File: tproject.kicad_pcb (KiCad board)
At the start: 2 copper layers, 28 parts, among them J1 USB_B_Micro, J2 Conn_01x04_Pin, J3 Conn_01x04_Pin, J4 Conn_01x04_Pin, SW1 SW_SPDT, U1 STM32F103C8T6, U2 AMS1117-3.3, Y1 16MHz

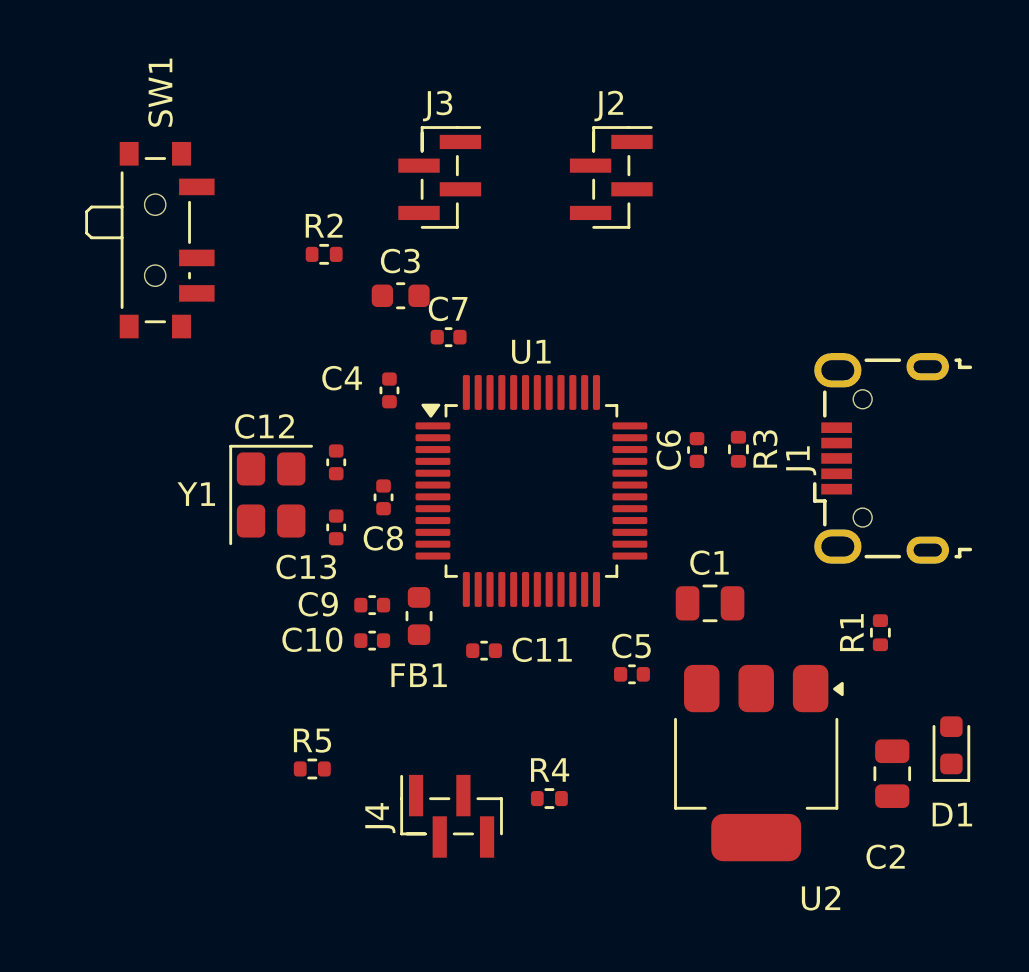
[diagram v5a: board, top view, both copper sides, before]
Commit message: Add board outline (38.54x33.17mm), 4x M2 mounting holes, adjust 8 components and add design note 0014
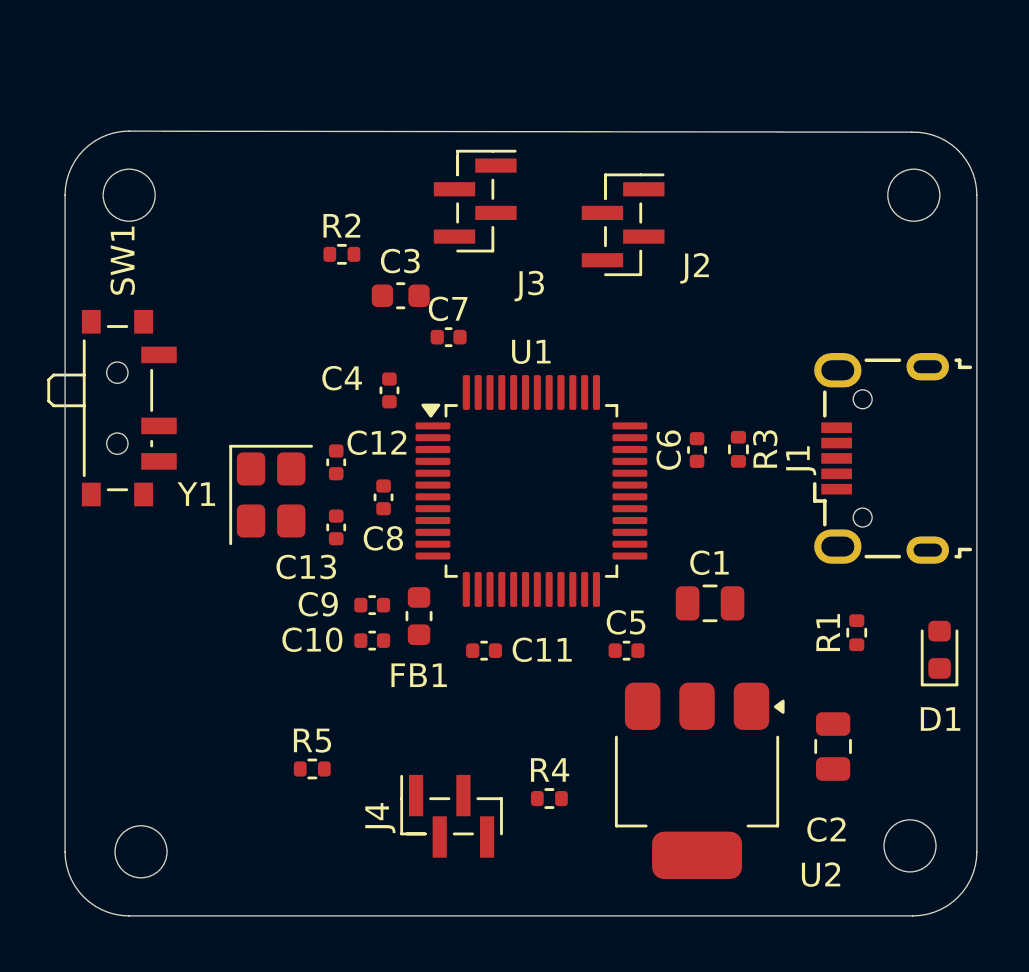
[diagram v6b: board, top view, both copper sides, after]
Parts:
- added H1: MountingHole, MountingHole:MountingHole_2.2mm_M2, F.Cu at (39.5, 82.5)
- added H2: MountingHole, MountingHole:MountingHole_2.2mm_M2, F.Cu at (39.0, 54.8)
- added H3: MountingHole, MountingHole:MountingHole_2.2mm_M2, F.Cu at (72.2, 54.8)
- added H4: MountingHole, MountingHole:MountingHole_2.2mm_M2, F.Cu at (72.0, 82.2)
- moved SW1 7.28 mm to (38.8, 63.8)
- moved D1 4.07 mm to (73.2, 74.0)
- moved C2 2.75 mm to (68.8, 78.0)
- moved U2 2.61 mm to (63.0, 79.5)
- moved J2 2.06 mm to (59.9, 56.0)
- moved J3 1.80 mm to (53.6, 55.0)
- moved C5 1.03 mm to (60.0, 74.0)
- moved R1 1.00 mm to (69.8, 73.2)
- moved R2 0.75 mm to (48.0, 57.2)
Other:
- board outline added: 38.5 x 33.2 mm

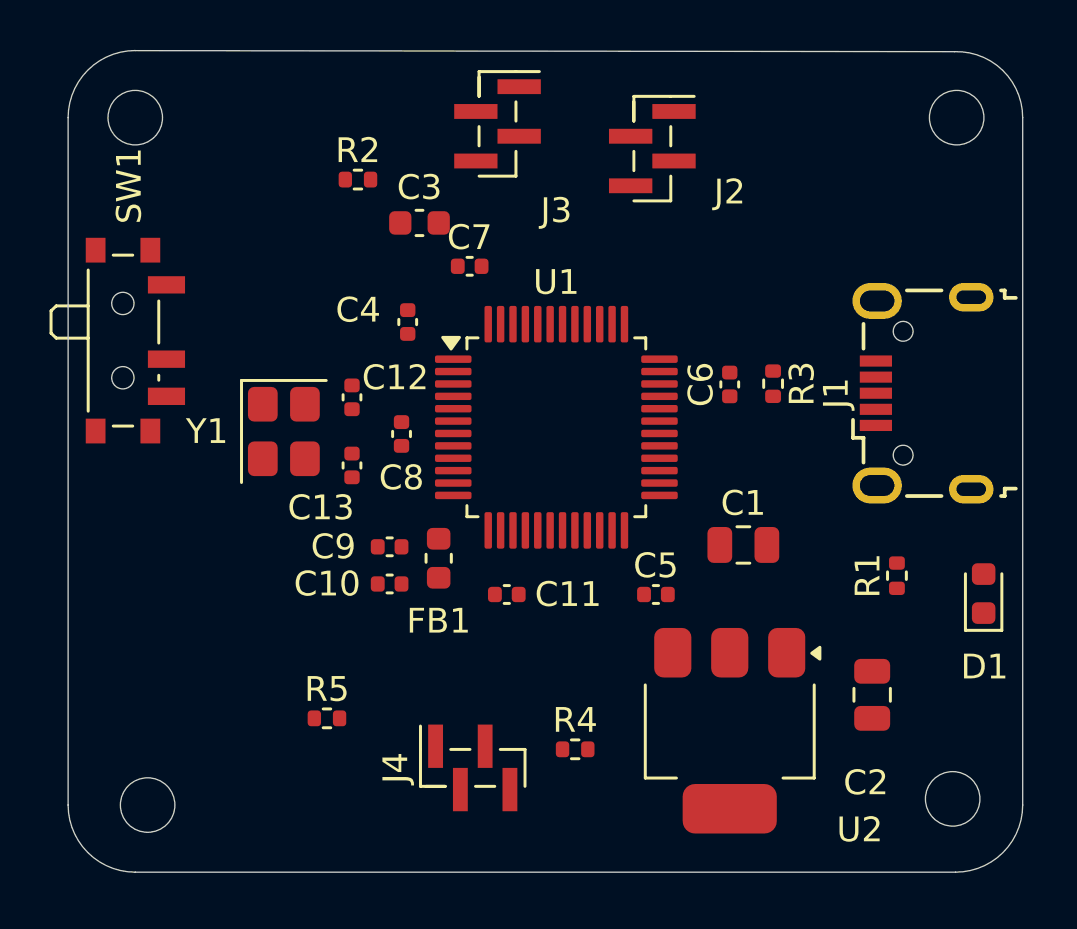
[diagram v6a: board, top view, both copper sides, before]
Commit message: Route decoupling caps and HSE crystal (39 tracks, B.Cu fill) and add design note 0015
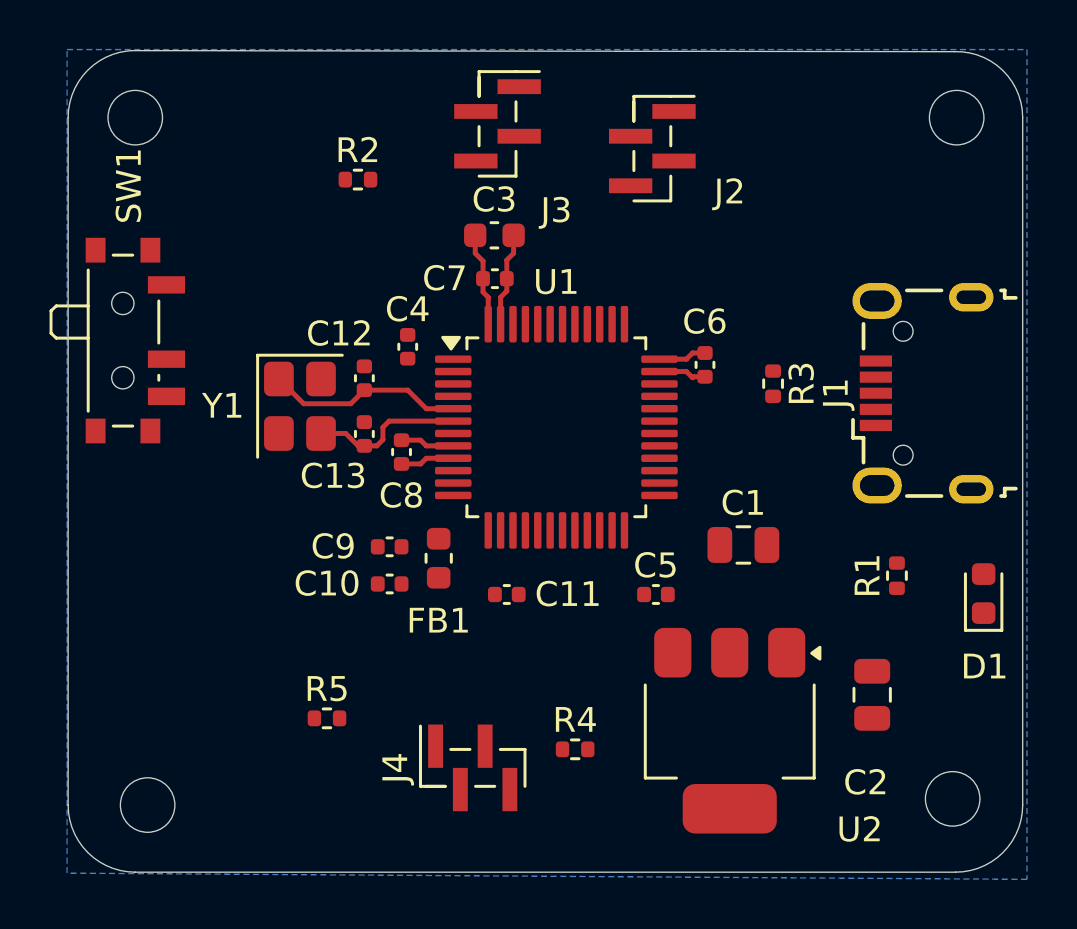
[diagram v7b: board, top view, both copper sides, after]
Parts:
- moved C3 3.07 mm to (53.5, 59.5)
- moved C13 1.36 mm to (48.2, 67.5)
- moved C6 1.27 mm to (62.0, 64.7), turned to -90 degrees
- moved Y1 1.21 mm to (45.6, 66.4)
- moved C7 1.14 mm to (53.5, 61.2)
- moved C4 1.00 mm to (50.0, 64.0)
- moved C12 0.92 mm to (48.2, 65.3)
- moved C8 0.73 mm to (49.8, 68.2)
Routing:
- net /HSE_IN: track 0.00 -> 7.99 mm
- net GND: track 0.00 -> 7.95 mm
- net /HSE_OUT: track 0.00 -> 6.25 mm
- net +3.3V: track 0.00 -> 5.75 mm
- net +3.3VA: track 0.00 -> 2.18 mm
- added copper zone on B.Cu, net (none)

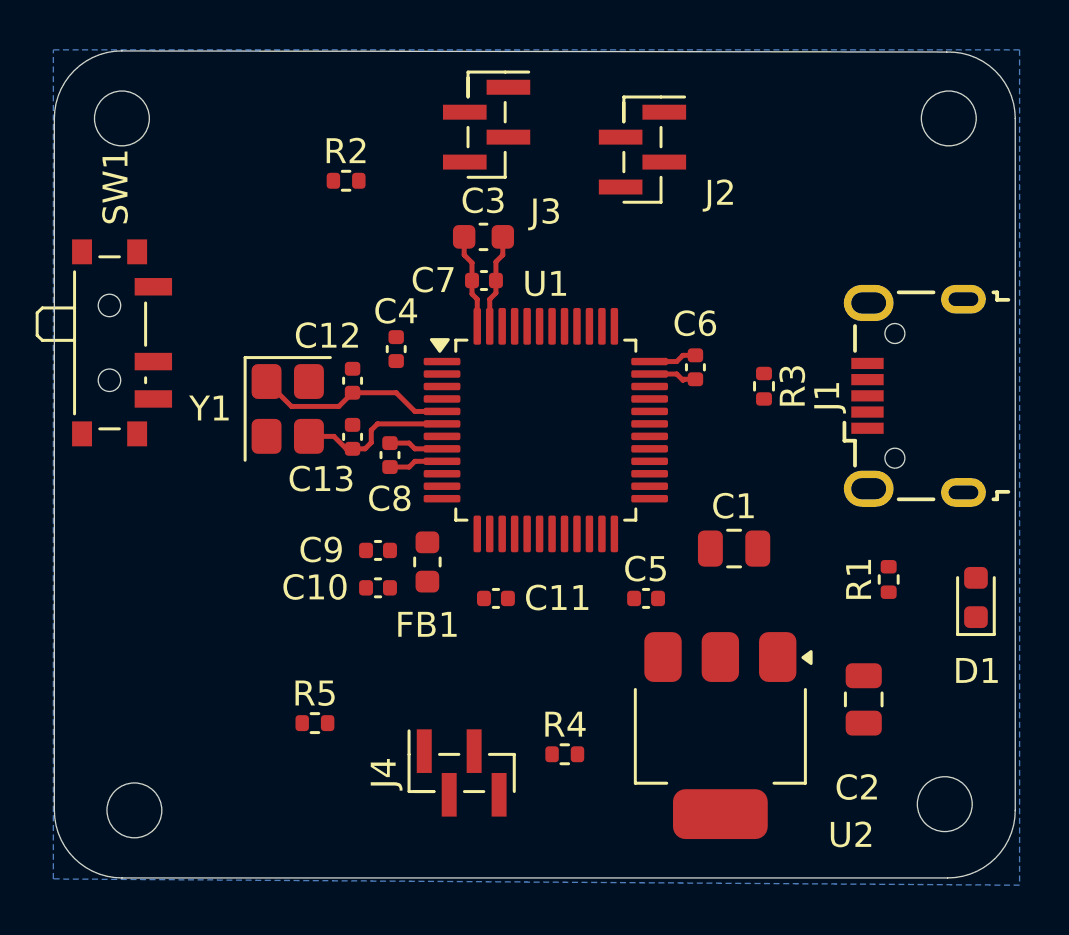
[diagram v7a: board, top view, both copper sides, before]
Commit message: Route all signal nets (52 segs, F.Cu) and add design note 0017
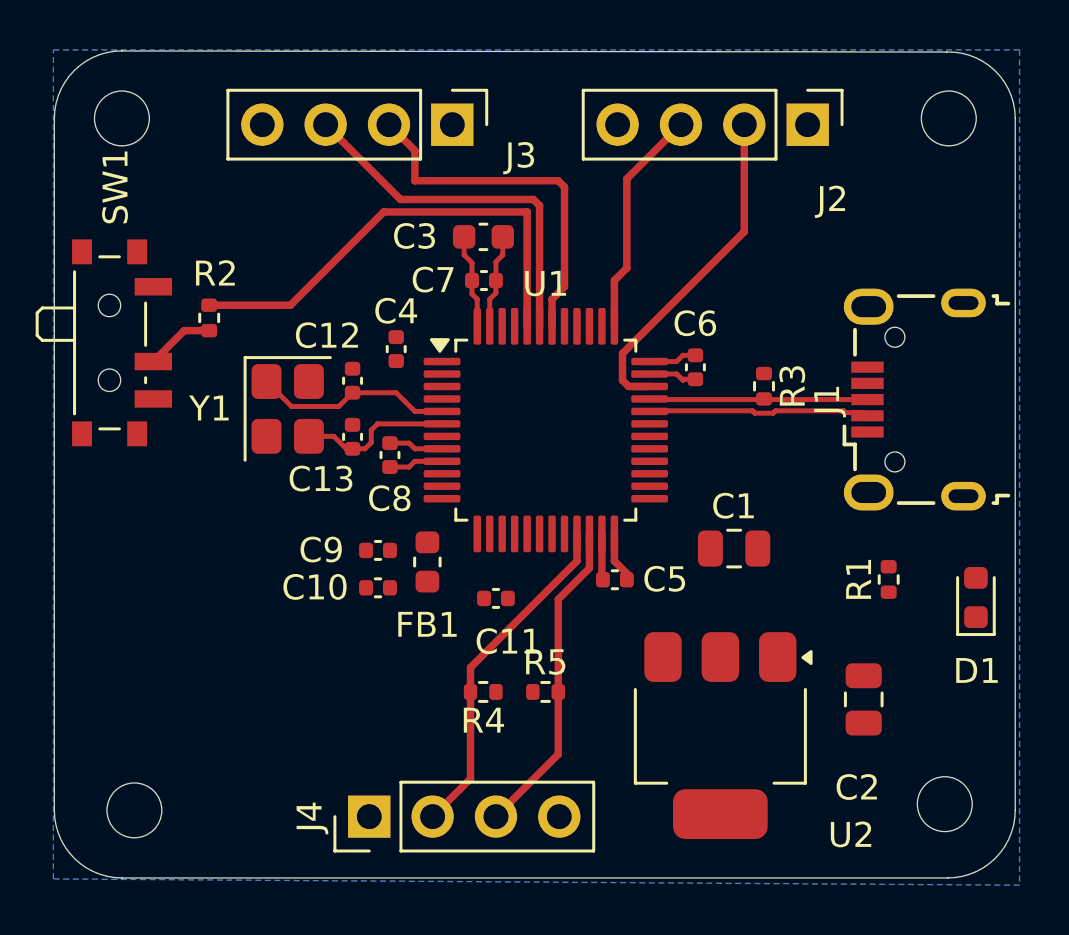
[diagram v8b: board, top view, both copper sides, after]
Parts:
- J2, J3, J4: footprint Connector_PinHeader_1.00mm:PinHeader_1x04_P1.00mm_Vertical_SMD_Pin1Right -> Connector_PinHeader_2.54mm:PinHeader_1x04_P2.54mm_Vertical
- moved R5 9.33 mm to (56.0, 77.8)
- moved R2 7.77 mm to (42.5, 62.8), turned to 90 degrees
- moved J2 6.70 mm to (66.5, 55.0), turned to -90 degrees
- moved R4 4.12 mm to (53.5, 77.8), turned to 180 degrees
- moved J4 4.10 mm to (48.9, 82.8)
- moved C5 1.46 mm to (58.8, 73.2), turned to 180 degrees
- moved J3 1.38 mm to (52.2, 55.0), turned to -90 degrees
- moved J1 0.15 mm to (70.8, 66.0)
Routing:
- net /BOOT0: track 0.00 -> 18.9 mm
- net /USART1_RX: track 0.00 -> 14.8 mm
- net /USART1_TX: track 0.00 -> 14.6 mm
- net /I2C2_SCL: track 0.00 -> 13.7 mm
- net /SDIO: track 0.00 -> 13.5 mm
- net /I2C2_SDA: track 0.00 -> 12.9 mm
- net /SWCLK: track 0.00 -> 9.19 mm
- net /USB_D-: track 0.00 -> 8.95 mm
- net /USB_D+: track 0.00 -> 8.75 mm
- net /SW_BOOT0: track 0.00 -> 2.75 mm
- net +3.3V: track 5.75 -> 7.79 mm
- net GND: track 7.95 -> 9.80 mm
